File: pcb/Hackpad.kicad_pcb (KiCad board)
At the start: 2 copper layers, 67 x 83 mm, 26 parts, among them J1 Conn_01x04_Pin, SW1 SW_Push_45deg, SW10 RotaryEncoder_Switch, SW2 SW_Push_45deg, SW3 SW_Push_45deg, SW4 SW_Push_45deg, SW5 SW_Push_45deg, SW6 SW_Push_45deg, SW7 SW_Push_45deg, SW8 SW_Push_45deg, SW9 SW_Push_45deg, U1 MOUDLE-SEEEDUINO-XIAO

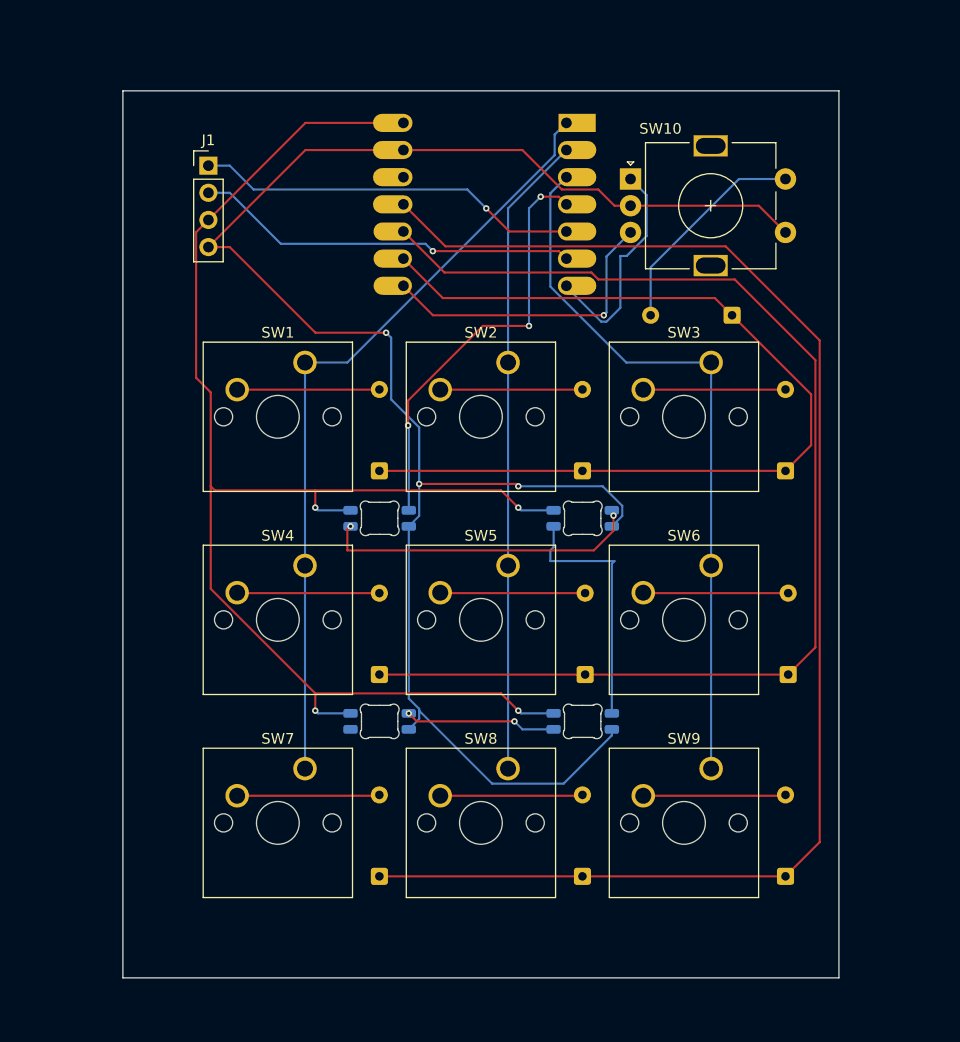
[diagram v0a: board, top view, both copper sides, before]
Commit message: updated pcb to include mounting screw holes
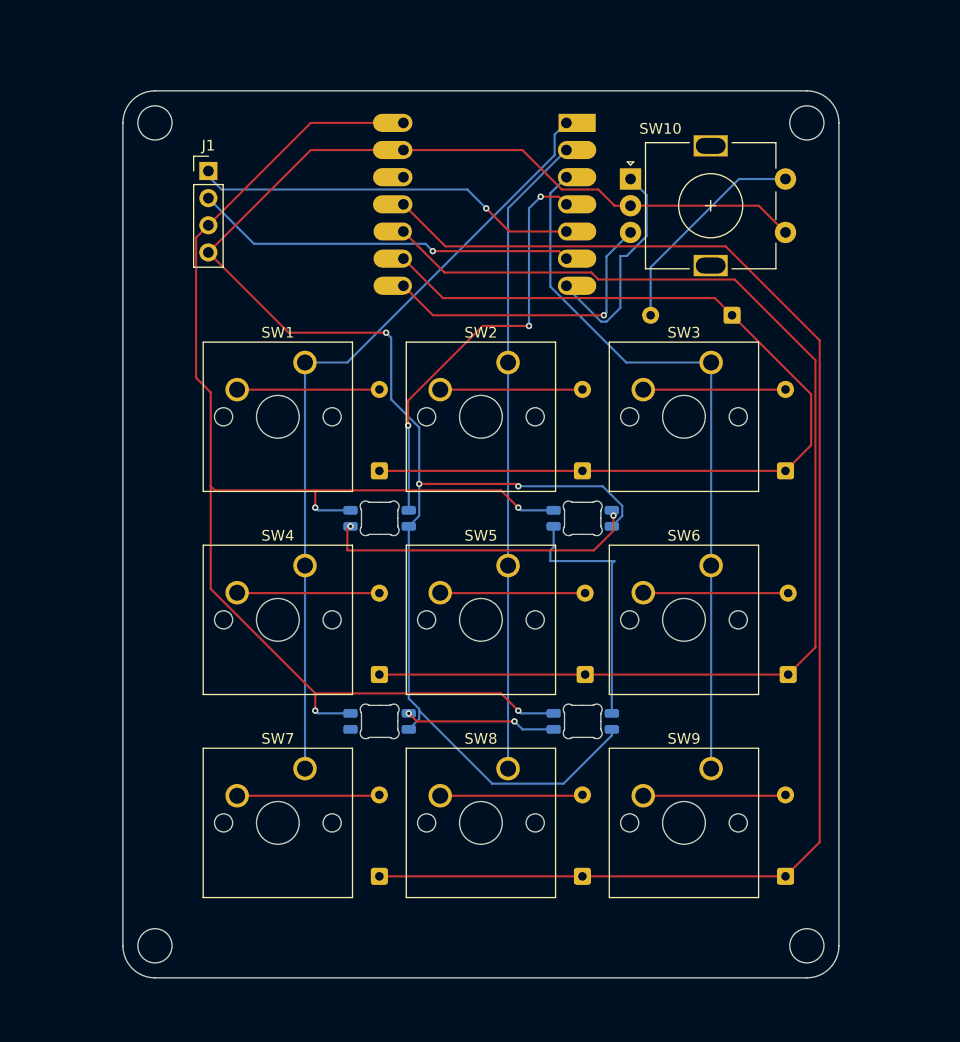
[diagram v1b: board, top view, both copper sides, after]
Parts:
- moved J1 0.50 mm to (111.0, 31.5)
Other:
- outline, holes or cut-outs redrawn

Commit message: Add files via upload
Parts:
- moved D14 7.50 mm to (152.5, 45.1), turned to 0 degrees
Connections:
- D14 pad 1: Row 0 -> BTN
- D14 pad 2: BTN -> Row 0
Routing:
- added copper zone on B.Cu, net (none)
- added copper zone on F.Cu, net (none)
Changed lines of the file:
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@@
 	(footprint "Diode_THT:D_DO-35_SOD27_P7.62mm_Horizontal"
 		(layer "B.Cu")
-		(at 160 45 180)
+		(at 152.5 45.1)
 		(descr "Diode, DO-35_SOD27 series, Axial, Horizontal, pin pitch=7.62mm, length*diameter=4*2mm^2, http://www.diodes.com/_files/packages/DO-35.pdf")
 		(tags "Diode DO-35_SOD27 series Axial Horizontal pin pitch 7.62mm  length 4mm diameter 2mm")
@@
 		)
 		(property "Sim.Device" "D"
-			(at 0 0 0)
+			(at 0 0 180)
 			(unlocked yes)
 			(layer "B.Fab")
@@
 		)
 		(property "Sim.Pins" "1=K 2=A"
-			(at 0 0 0)
+			(at 0 0 180)
 			(unlocked yes)
 			(layer "B.Fab")
@@
 		(duplicate_pad_numbers_are_jumpers no)
 		(fp_line
+			(start 1.04 0)
+			(end 1.69 0)
+			(stroke
+				(width 0.12)
+				(type solid)
+			)
+			(layer "B.SilkS")
+		)
+		(fp_line
+			(start 2.29 1.12)
+			(end 2.29 -1.12)
+			(stroke
+				(width 0.12)
+				(type solid)
+			)
+			(layer "B.SilkS")
+		)
+		(fp_line
+			(start 2.41 1.12)
+			(end 2.41 -1.12)
+			(stroke
+				(width 0.12)
+				(type solid)
+			)
+			(layer "B.SilkS")
+		)
+		(fp_line
+			(start 2.53 1.12)
+			(end 2.53 -1.12)
+			(stroke
+				(width 0.12)
+				(type solid)
+			)
+			(layer "B.SilkS")
+		)
+		(fp_line
 			(start 6.58 0)
 			(end 5.93 0)
-			(stroke
-				(width 0.12)
-				(type solid)
-			)
-			(layer "B.SilkS")
-		)
-		(fp_line
-			(start 2.53 1.12)
-			(end 2.53 -1.12)
-			(stroke
-				(width 0.12)
-				(type solid)
-			)
-			(layer "B.SilkS")
-		)
-		(fp_line
-			(start 2.41 1.12)
-			(end 2.41 -1.12)
-			(stroke
-				(width 0.12)
-				(type solid)
-			)
-			(layer "B.SilkS")
-		)
-		(fp_line
-			(start 2.29 1.12)
-			(end 2.29 -1.12)
-			(stroke
-				(width 0.12)
-				(type solid)
-			)
-			(layer "B.SilkS")
-		)
-		(fp_line
-			(start 1.04 0)
-			(end 1.69 0)
 			(stroke
 				(width 0.12)
@@
 		)
 		(fp_line
+			(start 0 0)
+			(end 1.81 0)
+			(stroke
+				(width 0.1)
+				(type solid)
+			)
+			(layer "B.Fab")
+		)
+		(fp_line
+			(start 2.31 1)
+			(end 2.31 -1)
+			(stroke
+				(width 0.1)
+				(type solid)
+			)
+			(layer "B.Fab")
+		)
+		(fp_line
+			(start 2.41 1)
+			(end 2.41 -1)
+			(stroke
+				(width 0.1)
+				(type solid)
+			)
+			(layer "B.Fab")
+		)
+		(fp_line
+			(start 2.51 1)
+			(end 2.51 -1)
+			(stroke
+				(width 0.1)
+				(type solid)
+			)
+			(layer "B.Fab")
+		)
+		(fp_line
 			(start 7.62 0)
 			(end 5.81 0)
-			(stroke
-				(width 0.1)
-				(type solid)
-			)
-			(layer "B.Fab")
-		)
-		(fp_line
-			(start 2.51 1)
-			(end 2.51 -1)
-			(stroke
-				(width 0.1)
-				(type solid)
-			)
-			(layer "B.Fab")
-		)
-		(fp_line
-			(start 2.41 1)
-			(end 2.41 -1)
-			(stroke
-				(width 0.1)
-				(type solid)
-			)
-			(layer "B.Fab")
-		)
-		(fp_line
-			(start 2.31 1)
-			(end 2.31 -1)
-			(stroke
-				(width 0.1)
-				(type solid)
-			)
-			(layer "B.Fab")
-		)
-		(fp_line
-			(start 0 0)
-			(end 1.81 0)
 			(stroke
 				(width 0.1)
@@
 			)
 		)
+		(fp_text user "K"
+			(at 0 1.8 0)
+			(layer "B.Fab")
+			(effects
+				(font
+					(size 1 1)
+					(thickness 0.15)
+				)
+				(justify mirror)
+			)
+		)
 		(fp_text user "${REFERENCE}"
 			(at 4.11 0 0)
@@
 			)
 		)
-		(fp_text user "K"
-			(at 0 1.8 0)
-			(layer "B.Fab")
-			(effects
-				(font
-					(size 1 1)
-					(thickness 0.15)
-				)
-				(justify mirror)
-			)
-		)
 		(pad "1" thru_hole roundrect
-			(at 0 0 180)
+			(at 0 0)
 			(size 1.6 1.6)
 			(drill 0.8)
@@
 			(remove_unused_layers no)
 			(roundrect_rratio 0.15625)
-			(net "Row 0")
+			(net "BTN")
 			(pinfunction "K_1")
 			(pintype "passive")
 		)
 		(pad "2" thru_hole circle
-			(at 7.62 0 180)
+			(at 7.62 0)
 			(size 1.6 1.6)
 			(drill 0.8)
 			(layers "*.Cu" "*.Mask")
 			(remove_unused_layers no)
-			(net "BTN")
+			(net "Row 0")
 			(pinfunction "A_2")
 			(pintype "passive")
@@
 		(net "Net-(D11-DOUT)")
 	)
+	(zone
+		(layers "F.Cu" "B.Cu")
+		(hatch edge 0.5)
+		(connect_pads
+			(clearance 0.5)
+		)
+		(min_thickness 0.25)
+		(fill yes
+			(thermal_gap 0.5)
+			(thermal_bridge_width 0.5)
+			(island_removal_mode 1)
+		)
+		(polygon
+			(pts
+				(xy 176.6 21.7) (xy 93.5 17.5) (xy 94.3 111) (xy 179.3 111)
+			)
+		)
+	)
 	(embedded_fonts no)
